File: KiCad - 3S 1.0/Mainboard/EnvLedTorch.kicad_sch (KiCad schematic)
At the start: 127 parts, among them IC1 BQ25792RQMR, IC2 TPS25750DRJKR, J1 USB_C_Receptacle_USB2.0, J10 3S/1.5MHz/1A ICGH, J11 4S/1.5MHz/1A ICGH, J2 Conn_01x02, J3 Aardvark, J4 SYS/GND, J5 BAT/GND, J6 Aardvark, J7 THERMISTOR / GND, J8 TS/NORM, J9 2S/1.5MHz/2A ICGH, Q1 BSP89, Q2 BSP89, Q3 BSP89, Q4 AO3401A, Q5 AO3401A, U1 HY2213, U2 HY2213, U3 HY2213, U4 TLV75533PDBV, U6 CAT24C256, U9 8254

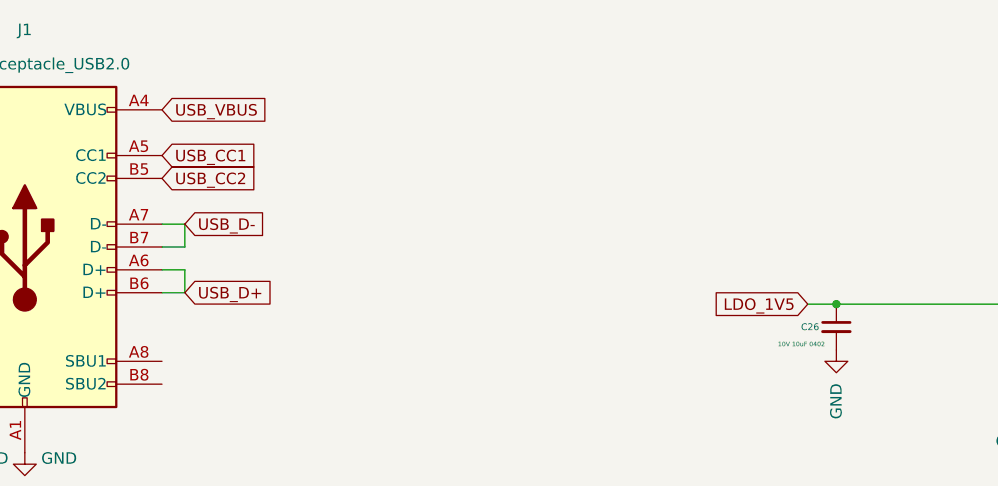
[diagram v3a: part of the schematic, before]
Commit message: added TVS2200 to schematic matching the reference design.
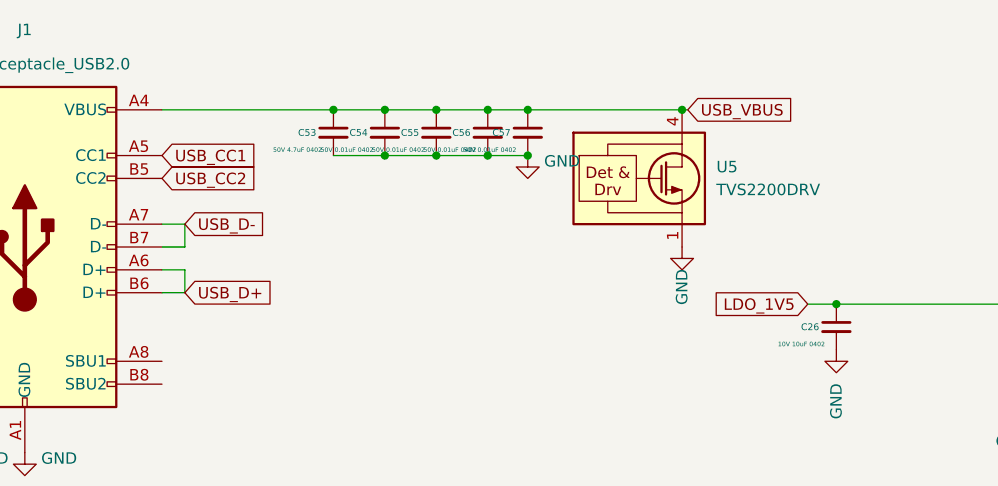
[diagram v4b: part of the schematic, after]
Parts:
- added C53: 50V 4.7uF 0402, Capacitor_SMD:C_0402_1005Metric, symbol Device:C_Small
- added C54, C55, C56, C57: 50V 0.01uF 0402, Capacitor_SMD:C_0402_1005Metric, symbol Device:C_Small
- added U5: TVS2200DRV, Package_SON:WSON-6-1EP_2x2mm_P0.65mm_EP1x1.6mm, symbol Power_Protection:TVS2200DRV
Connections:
- net GND: now also C53.2, C54.2, C55.2, C56.2, C57.2, U5.1 (GND), U5.2 (GND), U5.3 (GND), U5.7 (GND)
- net USB_VBUS: now also C53.1, C54.1, C55.1, C56.1, C57.1, U5.4 (IN), U5.5 (IN), U5.6 (IN)

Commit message: updated all symbols to match BOM
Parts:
- C12, C13, C31, C32, C33, C34, C37, C38: value 10uF 0402 -> 10uF 0603; footprint Capacitor_SMD:C_0402_1005Metric -> Capacitor_SMD:C_0603_1608Metric
- C14, C15: value 50V 4.7uF 0402 -> 50V 4.7uF 1210; footprint Capacitor_SMD:C_0402_1005Metric -> Capacitor_SMD:C_1210_3225Metric
- C16: value 50V 10nF 0402 -> 50V 10nF 1210; footprint Capacitor_SMD:C_0402_1005Metric -> Capacitor_SMD:C_1210_3225Metric
- C17: value 100V 10nF 0402 -> 100V 10nF 0603 X7R; footprint Capacitor_SMD:C_0402_1005Metric -> Capacitor_SMD:C_0603_1608Metric
- C19: value 50V 2.2nF 0402 -> 50V 2.2nF 0805; footprint Capacitor_SMD:C_0402_1005Metric -> Capacitor_SMD:C_0805_2012Metric
- C20: value 50V 22pF 0402 -> 50V 22pF 0603 C0G/NP0; footprint Capacitor_SMD:C_0402_1005Metric -> Capacitor_SMD:C_0603_1608Metric
- C21: value 6.3V 100uF 0402 -> TA 6.3V 100uF 1210; footprint Capacitor_SMD:C_0402_1005Metric -> Capacitor_SMD:C_1210_3225Metric
- C22, C23: value 10V 47uF 0402 -> 10V 47uF 1210; footprint Capacitor_SMD:C_0402_1005Metric -> Capacitor_SMD:C_1210_3225Metric
- C24, C25, C26: value 10V 10uF 0402 -> 10V 10uF 0402 X5R
- C27, C28: value 22uF 0402 -> 35V 22uF 0805 X5R; footprint Capacitor_SMD:C_0402_1005Metric -> Capacitor_SMD:C_0805_2012Metric
- C29: value 0.1uF 0402 -> 0.1uF 0402 X5R 35V
- C35: footprint Capacitor_SMD:C_0402_1005Metric -> Capacitor_SMD:C_0603_1608Metric
- C39: value 0.1uF 0402 -> 0.1uF 0603; footprint Capacitor_SMD:C_0402_1005Metric -> Capacitor_SMD:C_0603_1608Metric
- C40: value 4.7uF 0402 -> 4.7uF 0603; footprint Capacitor_SMD:C_0402_1005Metric -> Capacitor_SMD:C_0603_1608Metric
- C43, C45, C46, C47, C48: value 50V 10uF 0402 -> 50V 10uF 0805; footprint Capacitor_SMD:C_0402_1005Metric -> Capacitor_SMD:C_0805_2012Metric
- C50, C51: value 50V 10uF 0402 -> 50V 10uF 0603; footprint Capacitor_SMD:C_0402_1005Metric -> Capacitor_SMD:C_0603_1608Metric
- C53: value 50V 4.7uF 0402 -> 50V 4.7uF 0603 X5R; footprint Capacitor_SMD:C_0402_1005Metric -> Capacitor_SMD:C_0603_1608Metric
- C54, C55, C56, C57: value 50V 0.01uF 0402 -> 50V 0.01uF 0402 X7R
- D1: value CDBC540-G -> Diode, Schottky, 40 V, 5 A, SMC
- J1: value USB_C_Receptacle_USB2.0 -> HRO_TYPE-C-31-M-12
- R10: value 51.1 0402 -> 0603; footprint Resistor_SMD:R_0402_1005Metric -> Resistor_SMD:R_0603_1608Metric
- R11: value 10.2K 0402 -> 10.2K 0603; footprint Resistor_SMD:R_0402_1005Metric -> Resistor_SMD:R_0603_1608Metric
- R12: value 1.96K0402 -> 1.96K 0603; footprint Resistor_SMD:R_0402_1005Metric -> Resistor_SMD:R_0603_1608Metric
- R29: value 100 0402 -> 100 0603; footprint Resistor_SMD:R_0402_1005Metric -> Resistor_SMD:R_0603_1608Metric
- R32: value 10.0 0402 -> 10.0 1206; footprint Resistor_SMD:R_0402_1005Metric -> Resistor_SMD:R_1206_3216Metric
- R36: value 137K 0402 -> 137K 0603; footprint Resistor_SMD:R_0402_1005Metric -> Resistor_SMD:R_0603_1608Metric
- R37: value 100K 0402 -> 100K 0603; footprint Resistor_SMD:R_0402_1005Metric -> Resistor_SMD:R_0603_1608Metric
- R39: value 6.04K 0402 -> 6.04K 0603; footprint Resistor_SMD:R_0402_1005Metric -> Resistor_SMD:R_0603_1608Metric
- R40: value 10.5K 0402 -> 10.5K 0603; footprint Resistor_SMD:R_0402_1005Metric -> Resistor_SMD:R_0603_1608Metric
- R41: value 17.4K 0402 -> 17.4K 0603; footprint Resistor_SMD:R_0402_1005Metric -> Resistor_SMD:R_0603_1608Metric
- R7: value 665K 0402 -> 665K 0603; footprint Resistor_SMD:R_0402_1005Metric -> Resistor_SMD:R_0603_1608Metric
- R8: value 130K 0402 -> 130K 0603; footprint Resistor_SMD:R_0402_1005Metric -> Resistor_SMD:R_0603_1608Metric
- R9: value 37.4K 0402 -> 37.4K 0603; footprint Resistor_SMD:R_0402_1005Metric -> Resistor_SMD:R_0603_1608Metric
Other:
- moved on the sheet: C26, R13, R14

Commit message: updated inductors.
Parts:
- L1: value 4.7uH -> 9.5A 4.7uH 15m 1050; footprint Inductor_SMD:L_Sunlord_MWSA0804S -> Inductor_SMD:L_Wuerth_HCI-1050
- L2: value 1uH -> IHLP2020BZER1R0M11; footprint Inductor_SMD:L_0805_2012Metric -> Inductor_SMD:L_Vishay_IHLP-2020
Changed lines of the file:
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@@
       (effects (font (size 1.27 1.27)) (justify left))
     )
-    (property "Value" "1uH" (at 385.445 104.14 0)
+    (property "Value" "IHLP2020BZER1R0M11" (at 385.445 104.14 0)
       (effects (font (size 1.27 1.27)) (justify left))
     )
-    (property "Footprint" "Inductor_SMD:L_0805_2012Metric" (at 384.175 102.87 0)
+    (property "Footprint" "Inductor_SMD:L_Vishay_IHLP-2020" (at 384.175 102.87 0)
       (effects (font (size 1.27 1.27)) hide)
     )
@@
       (effects (font (size 1.27 1.27)))
     )
-    (property "Value" "4.7uH" (at 358.14 25.4 90)
+    (property "Value" "9.5A 4.7uH 15m 1050" (at 358.14 25.4 90)
       (effects (font (size 1.27 1.27)))
     )
-    (property "Footprint" "Inductor_SMD:L_Sunlord_MWSA0804S" (at 358.14 28.575 0)
+    (property "Footprint" "Inductor_SMD:L_Wuerth_HCI-1050" (at 358.14 28.575 0)
       (effects (font (size 1.27 1.27)) hide)
     )

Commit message: C35 had wrong footprint, changed from 0603 to 0402
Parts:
- C35: footprint Capacitor_SMD:C_0603_1608Metric -> Capacitor_SMD:C_0402_1005Metric
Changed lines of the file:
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@@
       (effects (font (size 0.5 0.5)) (justify left))
     )
-    (property "Footprint" "Capacitor_SMD:C_0603_1608Metric" (at 261.62 109.22 0)
+    (property "Footprint" "Capacitor_SMD:C_0402_1005Metric" (at 261.62 109.22 0)
       (effects (font (size 1.27 1.27)) hide)
     )

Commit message: few small corrections i forgot to commit
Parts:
- added C58, C59: 50V 10uF 0805, Capacitor_SMD:C_0805_2012Metric, symbol Device:C_Small
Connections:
- net GND: now also C58.2, C59.2
- net SYS: now also C58.1, C59.1
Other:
- moved on the sheet: J4
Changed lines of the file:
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@@
   (junction (at 368.935 157.48) (diameter 0) (color 0 0 0 0)
   )
+  (junction (at 385.445 127) (diameter 0) (color 0 0 0 0)
+  )
   (junction (at 147.955 97.155) (diameter 0) (color 0 0 0 0)
   )
@@
   (junction (at 147.955 92.075) (diameter 0) (color 0 0 0 0)
   )
+  (junction (at 385.445 121.92) (diameter 0) (color 0 0 0 0)
+  )
   (junction (at 102.235 263.525) (diameter 0) (color 0 0 0 0)
   )
@@
   (junction (at 381 28.575) (diameter 0) (color 0 0 0 0)
   )
-  (junction (at 376.555 121.92) (diameter 0) (color 0 0 0 0)
+  (junction (at 389.255 121.92) (diameter 0) (color 0 0 0 0)
   )
   (junction (at 389.89 28.575) (diameter 0) (color 0 0 0 0)
@@
   (junction (at 67.945 24.765) (diameter 0) (color 0 0 0 0)
   )
+  (junction (at 376.555 127) (diameter 0) (color 0 0 0 0)
+  )
   (junction (at 162.56 127.635) (diameter 0) (color 0 0 0 0)
   )
@@
   (junction (at 311.785 171.45) (diameter 0) (color 0 0 0 0)
   )
+  (junction (at 376.555 121.92) (diameter 0) (color 0 0 0 0)
+  )
   (junction (at 81.28 248.285) (diameter 0) (color 0 0 0 0)
   )
@@
     (stroke (width 0) (type default))
   )
-  (wire (pts (xy 376.555 121.92) (xy 368.3 121.92))
-    (stroke (width 0) (type default))
-  )
   (wire (pts (xy 372.11 197.485) (xy 372.11 194.31))
     (stroke (width 0) (type default))
@@
     (stroke (width 0) (type default))
   )
-  (wire (pts (xy 379.73 121.92) (xy 376.555 121.92))
+  (wire (pts (xy 392.43 121.92) (xy 389.255 121.92))
     (stroke (width 0) (type default))
   )
@@
     (stroke (width 0) (type default))
   )
-  (wire (pts (xy 379.73 124.46) (xy 376.555 124.46))
+  (wire (pts (xy 392.43 124.46) (xy 389.255 124.46))
     (stroke (width 0) (type default))
   )
@@
     (stroke (width 0) (type default))
   )
+  (wire (pts (xy 385.445 121.92) (xy 389.255 121.92))
+    (stroke (width 0) (type default))
+  )
   (wire (pts (xy 214.63 76.835) (xy 198.12 76.835))
     (stroke (width 0) (type default))
@@
     (stroke (width 0) (type default))
   )
-  (wire (pts (xy 376.555 124.46) (xy 376.555 121.92))
+  (wire (pts (xy 389.255 124.46) (xy 389.255 121.92))
     (stroke (width 0) (type default))
   )
@@
     (stroke (width 0) (type default))
   )
+  (wire (pts (xy 368.3 121.92) (xy 376.555 121.92))
+    (stroke (width 0) (type default))
+  )
   (wire (pts (xy 266.065 167.005) (xy 266.7 167.005))
     (stroke (width 0) (type default))
@@
     (stroke (width 0) (type default))
   )
+  (wire (pts (xy 376.555 127) (xy 385.445 127))
+    (stroke (width 0) (type default))
+  )
   (wire (pts (xy 271.78 129.54) (xy 282.575 129.54))
     (stroke (width 0) (type default))
@@
     (stroke (width 0) (type default))
   )
+  (wire (pts (xy 385.445 127) (xy 392.43 127))
+    (stroke (width 0) (type default))
+  )
   (wire (pts (xy 334.645 38.735) (xy 361.95 38.735))
     (stroke (width 0) (type default))
@@
     (stroke (width 0) (type default))
   )
+  (wire (pts (xy 368.3 127) (xy 376.555 127))
+    (stroke (width 0) (type default))
+  )
   (wire (pts (xy 270.51 177.8) (xy 266.7 177.8))
     (stroke (width 0) (type default))
@@
     (stroke (width 0) (type default))
   )
-  (wire (pts (xy 368.3 127) (xy 379.73 127))
-    (stroke (width 0) (type default))
-  )
   (wire (pts (xy 180.34 226.695) (xy 166.37 226.695))
     (stroke (width 0) (type default))
@@
     (stroke (width 0) (type default))
   )
+  (wire (pts (xy 376.555 121.92) (xy 385.445 121.92))
+    (stroke (width 0) (type default))
+  )
   (wire (pts (xy 43.18 42.545) (xy 45.72 42.545))
     (stroke (width 0) (type default))
@@
     )
   )
-  (global_label "SYS" (shape input) (at 379.73 121.92 0) (fields_autoplaced)
+  (global_label "SYS" (shape input) (at 392.43 121.92 0) (fields_autoplaced)
     (effects (font (size 1.27 1.27)) (justify left))
-    (property "Intersheetrefs" "${INTERSHEET_REFS}" (at 386.2228 121.92 0)
+    (property "Intersheetrefs" "${INTERSHEET_REFS}" (at 398.9228 121.92 0)
       (effects (font (size 1.27 1.27)) (justify left) hide)
     )
@@
     )
   )
+  (symbol (lib_id "Device:C_Small") (at 385.445 124.46 0) (unit 1)
+    (in_bom yes) (on_board yes) (dnp no)
+    (property "Reference" "C59" (at 387.35 124.46 0)
+      (effects (font (size 0.75 0.75)) (justify left))
+    )
+    (property "Value" "50V 10uF 0805" (at 386.715 126.365 0)
+      (effects (font (size 0.5 0.5)) (justify left))
+    )
+    (property "Footprint" "Capacitor_SMD:C_0805_2012Metric" (at 385.445 124.46 0)
+      (effects (font (size 1.27 1.27)) hide)
+    )
+    (property "Datasheet" "~" (at 385.445 124.46 0)
+      (effects (font (size 1.27 1.27)) hide)
+    )
+    (pin "1")
+    (pin "2")
+    (instances
+      (project "EnvLedTorch"
+        (path "/d80cef19-75ee-4cfe-8d31-e56b6cad8d97"
+          (reference "C59") (unit 1)
+        )
+      )
+    )
+  )
   (symbol (lib_id "power:GND") (at 272.415 119.38 0) (unit 1)
     (in_bom yes) (on_board yes) (dnp no) (fields_autoplaced)
@@
     )
   )
+  (symbol (lib_id "Device:C_Small") (at 376.555 124.46 0) (unit 1)
+    (in_bom yes) (on_board yes) (dnp no)
+    (property "Reference" "C58" (at 378.46 124.46 0)
+      (effects (font (size 0.75 0.75)) (justify left))
+    )
+    (property "Value" "50V 10uF 0805" (at 377.825 126.365 0)
+      (effects (font (size 0.5 0.5)) (justify left))
+    )
+    (property "Footprint" "Capacitor_SMD:C_0805_2012Metric" (at 376.555 124.46 0)
+      (effects (font (size 1.27 1.27)) hide)
+    )
+    (property "Datasheet" "~" (at 376.555 124.46 0)
+      (effects (font (size 1.27 1.27)) hide)
+    )
+    (pin "1")
+    (pin "2")
+    (instances
+      (project "EnvLedTorch"
+        (path "/d80cef19-75ee-4cfe-8d31-e56b6cad8d97"
+          (reference "C58") (unit 1)
+        )
+      )
+    )
+  )
   (symbol (lib_id "Transistor_FET:AO3401A") (at 58.42 196.85 270) (mirror x) (unit 1)
     (in_bom yes) (on_board yes) (dnp no) (fields_autoplaced)
@@
     )
   )
-  (symbol (lib_id "Connector_Generic:Conn_01x02") (at 384.81 124.46 0) (unit 1)
+  (symbol (lib_id "Connector_Generic:Conn_01x02") (at 397.51 124.46 0) (unit 1)
     (in_bom yes) (on_board yes) (dnp no) (fields_autoplaced)
-    (property "Reference" "J4" (at 387.35 124.46 0)
+    (property "Reference" "J4" (at 400.05 124.46 0)
       (effects (font (size 1.27 1.27)) (justify left))
     )
-    (property "Value" "SYS/GND" (at 387.35 127 0)
+    (property "Value" "SYS/GND" (at 400.05 127 0)
       (effects (font (size 1.27 1.27)) (justify left))
     )
-    (property "Footprint" "Connector_PinHeader_2.54mm:PinHeader_1x02_P2.54mm_Vertical" (at 384.81 124.46 0)
+    (property "Footprint" "Connector_PinHeader_2.54mm:PinHeader_1x02_P2.54mm_Vertical" (at 397.51 124.46 0)
       (effects (font (size 1.27 1.27)) hide)
     )
-    (property "Datasheet" "~" (at 384.81 124.46 0)
+    (property "Datasheet" "~" (at 397.51 124.46 0)
       (effects (font (size 1.27 1.27)) hide)
     )
